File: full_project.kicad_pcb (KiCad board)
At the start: 2 copper layers, 61.4 x 86.1 mm, 38 parts, among them J1 Conn_01x12, J12 V_OFFSET, J14 Conn_01x02, J2 Raspberry_Pi_2_3, J3 Conn_01x08, J4 Screw_Terminal_01x04_titrator, J5 RF_Shield_Two_Pieces, J6 BNC_Jack, J7 Conn_01x02, J8 Screw_Terminal_01x03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

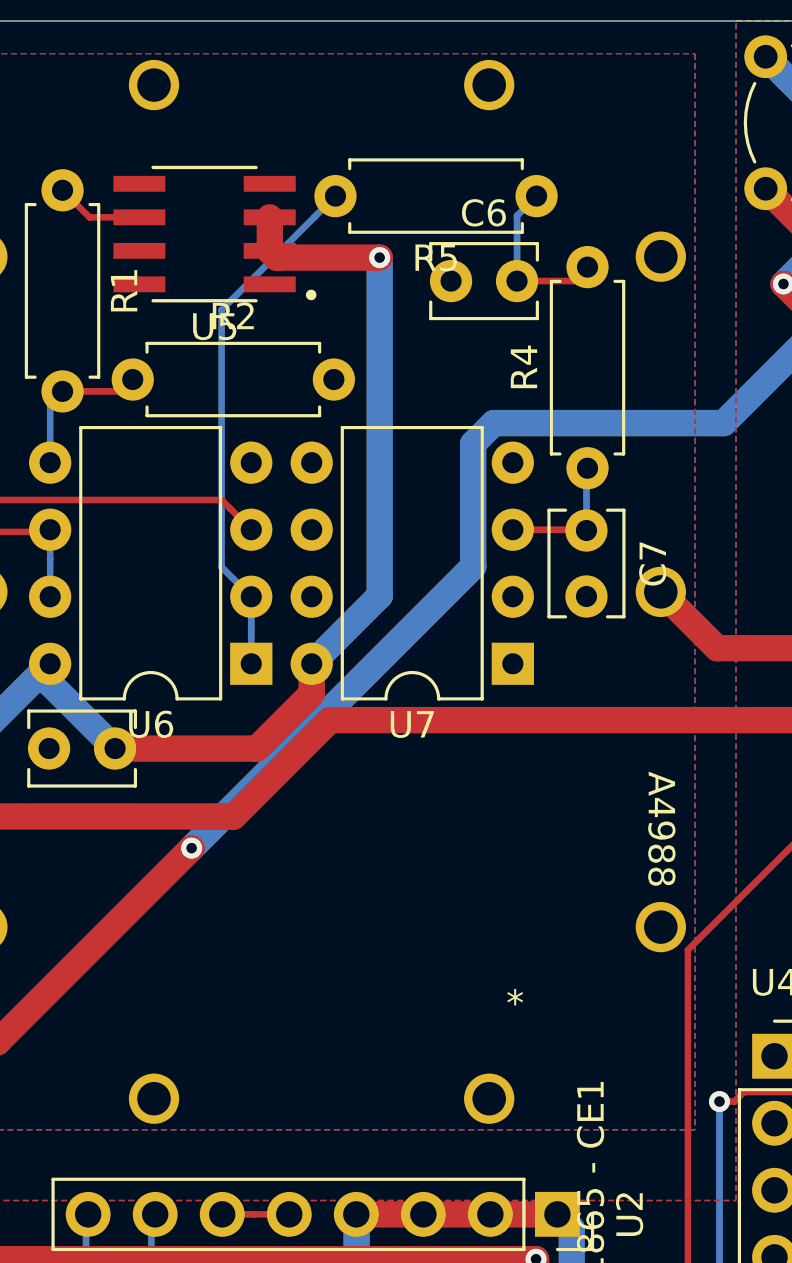
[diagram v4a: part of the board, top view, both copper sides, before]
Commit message: added low pass filter fix on schematic and pcb
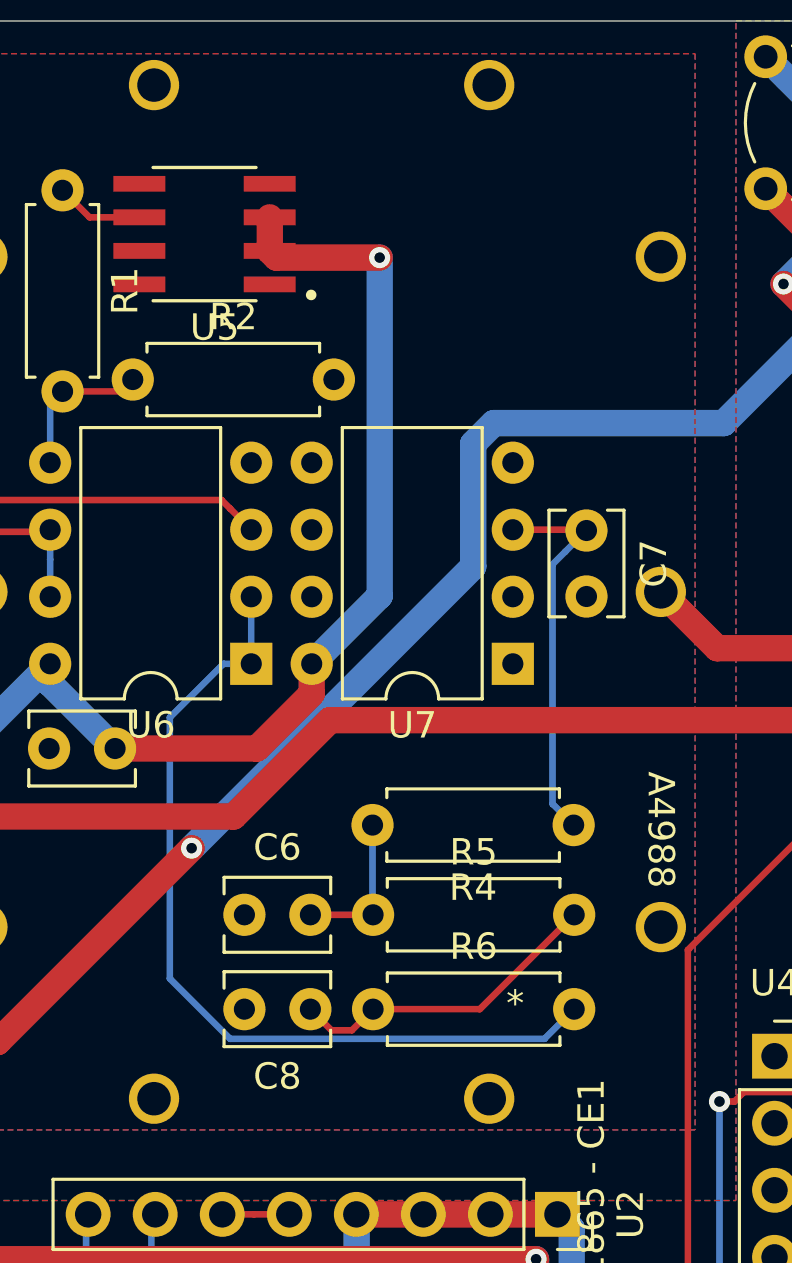
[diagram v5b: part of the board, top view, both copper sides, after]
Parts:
- added C8: 1uF, Capacitor_THT:C_Disc_D3.8mm_W2.6mm_P2.50mm, F.Cu at (151.1, 94.1)
- added R6: 80k, Resistor_THT:R_Axial_DIN0207_L6.3mm_D2.5mm_P7.62mm_Horizontal, F.Cu at (153.5, 94.1)
- R4: value 160000 -> 160k
- R5: value 160000 -> 80k
- moved R5 27.9 mm to (153.5, 90.5), turned to 0 degrees
- moved C6 25.3 mm to (148.6, 90.5)
- moved R4 13.5 mm to (161.1, 87.1), turned to 180 degrees
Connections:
- A1 pad 1: (no net) -> Net-(A1-Pad1)
- A1 pad 10: (no net) -> Net-(A1-Pad10)
- A1 pad 11: (no net) -> Net-(A1-Pad11)
- A1 pad 12: (no net) -> Net-(A1-Pad12)
- A1 pad 13: (no net) -> Net-(A1-Pad13)
- A1 pad 14: (no net) -> Net-(A1-Pad14)
- A1 pad 15: (no net) -> Net-(A1-Pad15)
- A1 pad 16: (no net) -> Net-(A1-Pad16)
- A1 pad 18: (no net) -> Net-(A1-Pad18)
- A1 pad 19: (no net) -> Net-(A1-Pad19)
- A1 pad 2: (no net) -> Net-(A1-Pad2)
- A1 pad 20: (no net) -> Net-(A1-Pad20)
- A1 pad 21: (no net) -> Net-(A1-Pad21)
- A1 pad 22: (no net) -> Net-(A1-Pad22)
- A1 pad 23: (no net) -> Net-(A1-Pad23)
- A1 pad 24: (no net) -> Net-(A1-Pad24)
- A1 pad 25: (no net) -> Net-(A1-Pad25)
- A1 pad 26: (no net) -> Net-(A1-Pad26)
- A1 pad 27: (no net) -> Net-(A1-Pad27)
- A1 pad 28: (no net) -> Net-(A1-Pad28)
- A1 pad 3: (no net) -> Net-(A1-Pad3)
- A1 pad 30: (no net) -> Net-(A1-Pad30)
- A1 pad 7: (no net) -> Net-(A1-Pad7)
- A1 pad 8: (no net) -> Net-(A1-Pad8)
- A1 pad 9: (no net) -> Net-(A1-Pad9)
- J2 pad 10: (no net) -> Net-(J2-Pad10)
- J2 pad 11: (no net) -> Net-(J2-Pad11)
- J2 pad 27: (no net) -> Net-(J2-Pad27)
- J2 pad 29: (no net) -> Net-(J2-Pad29)
- J2 pad 7: (no net) -> Net-(J2-Pad7)
- J2 pad 8: (no net) -> Net-(J2-Pad8)
- J6 pad 3: (no net) -> Net-(J6-Pad3)
- J6 pad 4: (no net) -> Net-(J6-Pad4)
- R5 pad 2: Net-(R5-Pad2) -> Net-(C8-Pad1)
- U1 pad 10: (no net) -> Net-(U1-Pad10)
- U1 pad 9: (no net) -> Net-(U1-Pad9)
- U3 pad 3: (no net) -> Net-(U3-Pad3)
- U3 pad 8: (no net) -> Net-(U3-Pad8)
- U4 pad 3: (no net) -> Net-(U4-Pad3)
- U4 pad 8: (no net) -> Net-(U4-Pad8)
- U5 pad 5: (no net) -> Net-(U5-Pad5)
- U6 pad 1: Net-(R5-Pad2) -> Net-(R6-Pad2)
- U6 pad 2: Net-(R5-Pad2) -> Net-(R6-Pad2)
- U7 pad 5: (no net) -> Net-(U7-Pad5)
- U7 pad 6: (no net) -> Net-(U7-Pad6)
- U7 pad 7: (no net) -> Net-(U7-Pad7)
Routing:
- net Net-(R6-Pad2): track 0.00 -> 33.1 mm
- net Net-(R5-Pad2): track 20.0 -> 0.00 mm
- net Net-(C8-Pad1): track 0.00 -> 12.1 mm
- net Net-(C7-Pad1): track 5.18 -> 14.8 mm
- net Net-(C6-Pad2): track 6.42 -> 5.78 mm
